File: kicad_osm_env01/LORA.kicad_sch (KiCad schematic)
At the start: 14 parts

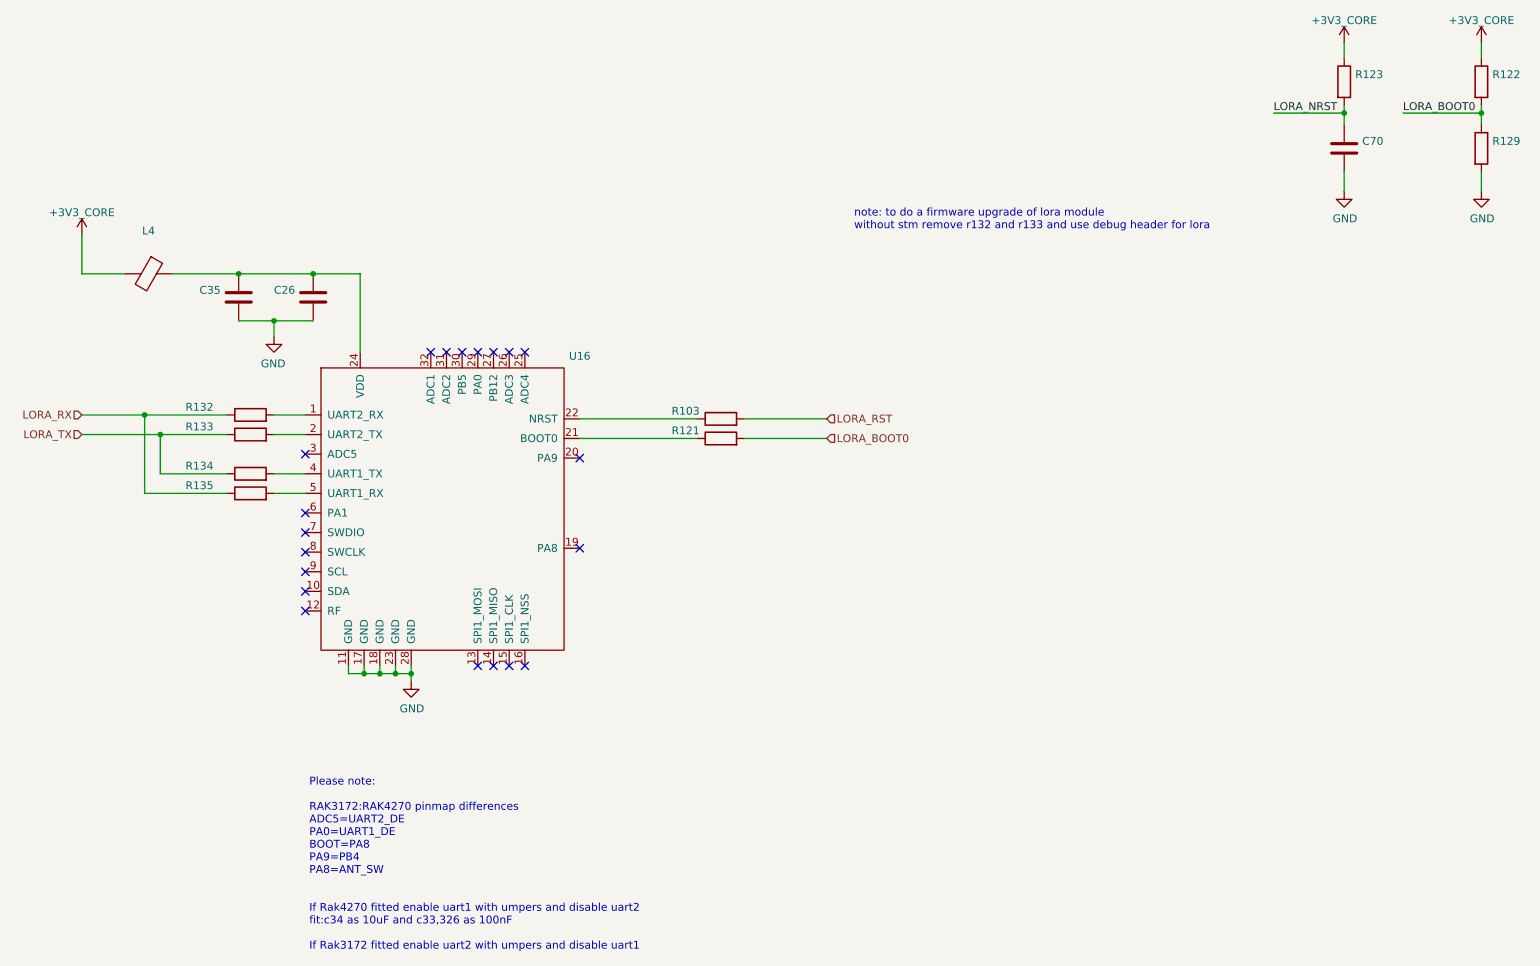
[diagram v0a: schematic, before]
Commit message: majority of signals routed on layout
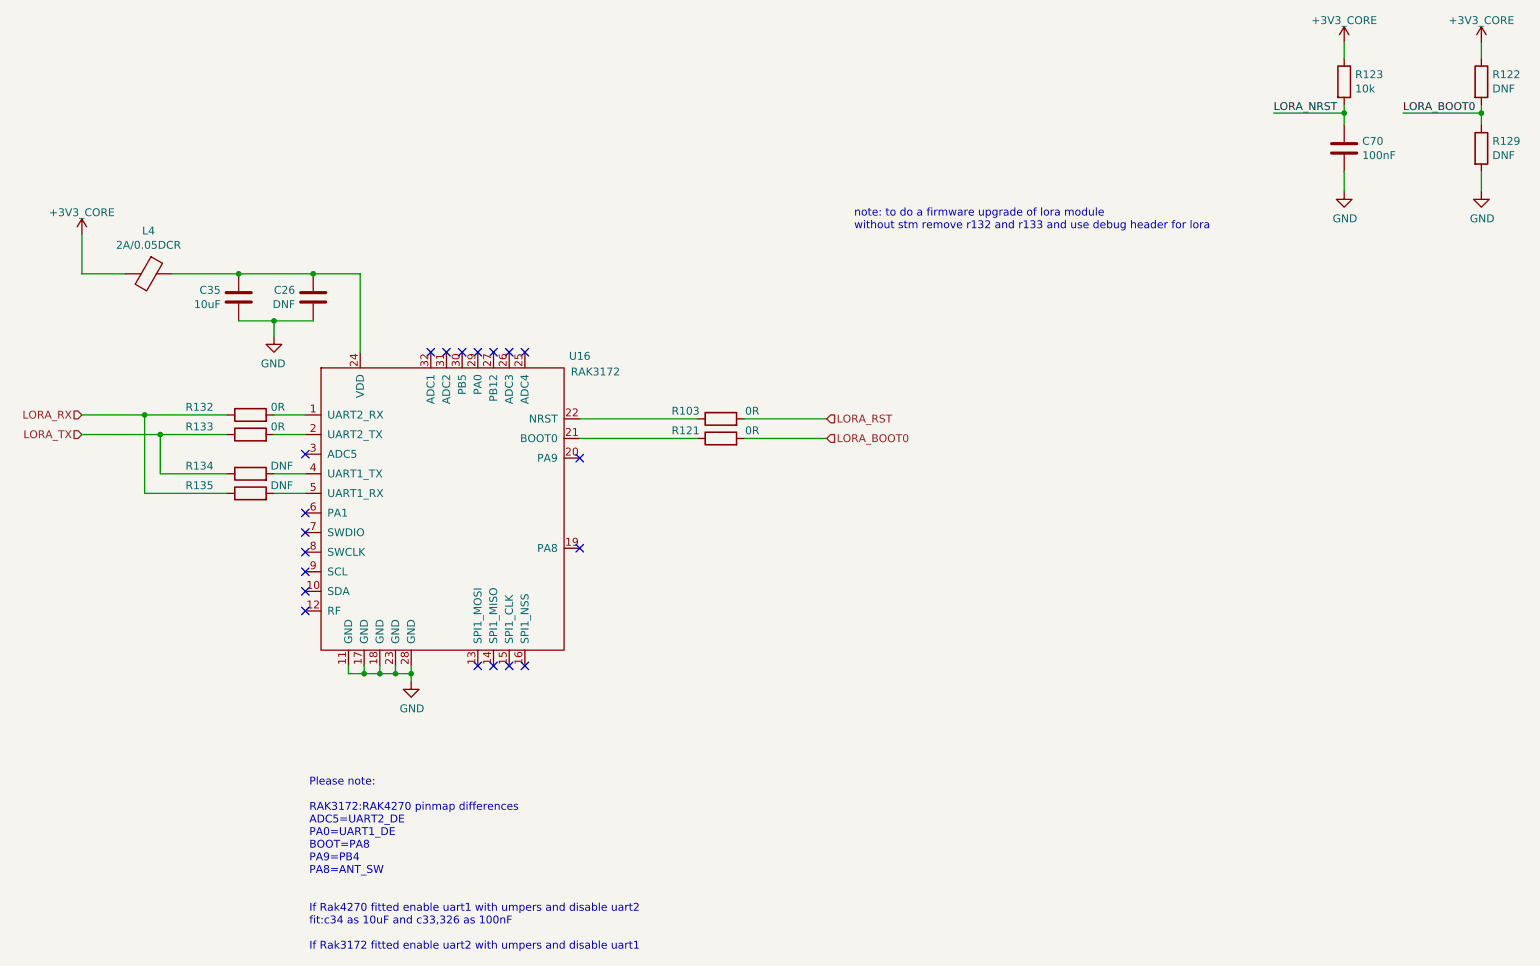
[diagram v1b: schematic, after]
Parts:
- C26: value (none) -> DNF; footprint (none) -> Capacitor_SMD:C_0402_1005Metric
- C35: value (none) -> 10uF; footprint (none) -> Capacitor_SMD:C_0603_1608Metric
- C70: value (none) -> 100nF; footprint (none) -> Capacitor_SMD:C_0402_1005Metric
- L4: value (none) -> 2A/0.05DCR; footprint (none) -> Inductor_SMD:L_0402_1005Metric
- R103, R121, R132, R133: value (none) -> 0R; footprint (none) -> Resistor_SMD:R_0603_1608Metric
- R122, R129, R134, R135: value (none) -> DNF; footprint (none) -> Resistor_SMD:R_0603_1608Metric
- R123: value (none) -> 10k; footprint (none) -> Resistor_SMD:R_0603_1608Metric
- U16: value (none) -> RAK3172; footprint (none) -> Devtank_PCB_lib:RAK3172
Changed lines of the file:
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@@
       (effects (font (size 1.27 1.27)) (justify left))
     )
-    (property "Value" "" (id 1) (at 250.063 29.083 0)
-      (effects (font (size 1.27 1.27)) (justify left))
-    )
-    (property "Footprint" "" (id 2) (at 246.507 27.94 90)
+    (property "Value" "10k" (id 1) (at 250.063 29.083 0)
+      (effects (font (size 1.27 1.27)) (justify left))
+    )
+    (property "Footprint" "Resistor_SMD:R_0603_1608Metric" (id 2) (at 246.507 27.94 90)
       (effects (font (size 1.27 1.27)) hide)
     )
@@
       (effects (font (size 1.27 1.27)) (justify left))
     )
-    (property "Value" "" (id 1) (at 251.206 39.878 0)
-      (effects (font (size 1.27 1.27)) (justify left))
-    )
-    (property "Footprint" "" (id 2) (at 249.2502 42.545 0)
+    (property "Value" "100nF" (id 1) (at 251.206 39.878 0)
+      (effects (font (size 1.27 1.27)) (justify left))
+    )
+    (property "Footprint" "Capacitor_SMD:C_0402_1005Metric" (id 2) (at 249.2502 42.545 0)
       (effects (font (size 1.27 1.27)) hide)
     )
@@
       (effects (font (size 1.27 1.27)) (justify left))
     )
-    (property "Value" "" (id 1) (at 78.359 64.008 0)
-      (effects (font (size 1.27 1.27)) (justify left))
-    )
-    (property "Footprint" "" (id 2) (at 80.3148 66.675 0)
+    (property "Value" "DNF" (id 1) (at 78.359 64.008 0)
+      (effects (font (size 1.27 1.27)) (justify left))
+    )
+    (property "Footprint" "Capacitor_SMD:C_0402_1005Metric" (id 2) (at 80.3148 66.675 0)
       (effects (font (size 1.27 1.27)) hide)
     )
@@
       (effects (font (size 1.27 1.27)) (justify left))
     )
-    (property "Value" "" (id 1) (at 66.294 64.008 0)
-      (effects (font (size 1.27 1.27)) (justify left))
-    )
-    (property "Footprint" "" (id 2) (at 68.2498 66.675 0)
+    (property "Value" "10uF" (id 1) (at 66.294 64.008 0)
+      (effects (font (size 1.27 1.27)) (justify left))
+    )
+    (property "Footprint" "Capacitor_SMD:C_0603_1608Metric" (id 2) (at 68.2498 66.675 0)
       (effects (font (size 1.27 1.27)) hide)
     )
@@
     (in_bom yes) (on_board yes)
     (property "Reference" "L4" (id 0) (at 54.61 52.0954 90))
-    (property "Value" "" (id 1) (at 54.61 54.4068 90))
-    (property "Footprint" "" (id 2) (at 54.61 57.277 90)
+    (property "Value" "2A/0.05DCR" (id 1) (at 54.61 54.4068 90))
+    (property "Footprint" "Inductor_SMD:L_0402_1005Metric" (id 2) (at 54.61 57.277 90)
       (effects (font (size 1.27 1.27)) hide)
     )
@@
     (in_bom yes) (on_board yes)
     (property "Reference" "R103" (id 0) (at 141.605 81.28 90))
-    (property "Value" "" (id 1) (at 152.4 81.28 90))
-    (property "Footprint" "" (id 2) (at 147.32 84.328 90)
+    (property "Value" "0R" (id 1) (at 152.4 81.28 90))
+    (property "Footprint" "Resistor_SMD:R_0603_1608Metric" (id 2) (at 147.32 84.328 90)
       (effects (font (size 1.27 1.27)) hide)
     )
@@
     (in_bom yes) (on_board yes)
     (property "Reference" "R135" (id 0) (at 62.865 93.345 90))
-    (property "Value" "" (id 1) (at 76.2 93.345 90))
-    (property "Footprint" "" (id 2) (at 71.12 96.393 90)
+    (property "Value" "DNF" (id 1) (at 76.2 93.345 90))
+    (property "Footprint" "Resistor_SMD:R_0603_1608Metric" (id 2) (at 71.12 96.393 90)
       (effects (font (size 1.27 1.27)) hide)
     )
@@
     (in_bom yes) (on_board yes)
     (property "Reference" "R132" (id 0) (at 62.865 80.645 90))
-    (property "Value" "" (id 1) (at 75.565 80.645 90))
-    (property "Footprint" "" (id 2) (at 71.12 83.693 90)
+    (property "Value" "0R" (id 1) (at 75.565 80.645 90))
+    (property "Footprint" "Resistor_SMD:R_0603_1608Metric" (id 2) (at 71.12 83.693 90)
       (effects (font (size 1.27 1.27)) hide)
     )
@@
       (effects (font (size 1.27 1.27)) (justify left))
     )
-    (property "Value" "" (id 1) (at 272.288 39.878 0)
-      (effects (font (size 1.27 1.27)) (justify left))
-    )
-    (property "Footprint" "" (id 2) (at 268.732 38.735 90)
+    (property "Value" "DNF" (id 1) (at 272.288 39.878 0)
+      (effects (font (size 1.27 1.27)) (justify left))
+    )
+    (property "Footprint" "Resistor_SMD:R_0603_1608Metric" (id 2) (at 268.732 38.735 90)
       (effects (font (size 1.27 1.27)) hide)
     )
@@
     (in_bom yes) (on_board yes)
     (property "Reference" "U16" (id 0) (at 124.46 72.39 0))
-    (property "Value" "" (id 1) (at 127 74.93 0))
-    (property "Footprint" "" (id 2) (at 95.885 85.09 0)
+    (property "Value" "RAK3172" (id 1) (at 127 74.93 0))
+    (property "Footprint" "Devtank_PCB_lib:RAK3172" (id 2) (at 95.885 85.09 0)
       (effects (font (size 1.27 1.27)) hide)
     )
@@
     (in_bom yes) (on_board yes)
     (property "Reference" "R134" (id 0) (at 62.865 90.17 90))
-    (property "Value" "" (id 1) (at 76.2 90.17 90))
-    (property "Footprint" "" (id 2) (at 71.12 93.218 90)
+    (property "Value" "DNF" (id 1) (at 76.2 90.17 90))
+    (property "Footprint" "Resistor_SMD:R_0603_1608Metric" (id 2) (at 71.12 93.218 90)
       (effects (font (size 1.27 1.27)) hide)
     )
@@
       (effects (font (size 1.27 1.27)) (justify left))
     )
-    (property "Value" "" (id 1) (at 272.288 29.083 0)
-      (effects (font (size 1.27 1.27)) (justify left))
-    )
-    (property "Footprint" "" (id 2) (at 268.732 27.94 90)
+    (property "Value" "DNF" (id 1) (at 272.288 29.083 0)
+      (effects (font (size 1.27 1.27)) (justify left))
+    )
+    (property "Footprint" "Resistor_SMD:R_0603_1608Metric" (id 2) (at 268.732 27.94 90)
       (effects (font (size 1.27 1.27)) hide)
     )
@@
     (in_bom yes) (on_board yes)
     (property "Reference" "R133" (id 0) (at 62.865 83.82 90))
-    (property "Value" "" (id 1) (at 75.565 83.82 90))
-    (property "Footprint" "" (id 2) (at 71.12 86.868 90)
+    (property "Value" "0R" (id 1) (at 75.565 83.82 90))
+    (property "Footprint" "Resistor_SMD:R_0603_1608Metric" (id 2) (at 71.12 86.868 90)
       (effects (font (size 1.27 1.27)) hide)
     )
@@
     (in_bom yes) (on_board yes)
     (property "Reference" "R121" (id 0) (at 141.605 84.455 90))
-    (property "Value" "" (id 1) (at 152.4 84.455 90))
-    (property "Footprint" "" (id 2) (at 147.32 87.503 90)
-      (effects (font (size 1.27 1.27)) hide)
-    )
+    (property "Value" "0R" (id 1) (at 152.4 84.455 90))
+    (property "Footprint" "Resistor_SMD:R_0603_1608Metric" (id 2) (at 147.32 87.503 90)
+      (effects (font (size 1.27 1.27)) hide)
+    )
